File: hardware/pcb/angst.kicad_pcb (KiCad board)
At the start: 2 copper layers, 50.8 x 50.8 mm, 86 parts, among them J1 USB_B_Micro, J2 Conn_02x05_Odd_Even, J3 Conn_01x02_Male, J4 Conn_01x03, J5 Conn_01x03, J6 Conn_01x03, J7 Conn_01x02_Male, J8 Conn_01x04_Male, J9 Conn_01x02_Male, Q1 IRLML6401TRPBF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

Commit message: Add initial placement of components on layout
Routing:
- net PC0: track 24.6 -> 0.22 mm, vias 2 -> 0
- net /OUTV_1: track 18.3 -> 0.00 mm, vias 2 -> 0
- net /OUTU_1: track 12.1 -> 0.00 mm
- net /OUTW_1: track 10.6 -> 0.00 mm
- net Net-(R12-Pad1): track 7.73 -> 0.23 mm
- net PA4: track 0.00 -> 5.08 mm
- net PA5: track 0.00 -> 5.04 mm
- net PA6: track 0.00 -> 5.00 mm
- net PA7: track 0.00 -> 4.96 mm
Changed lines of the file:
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@@
     (thickness 1.6)
     (drawings 4)
-    (tracks 34)
+    (tracks 6)
     (zones 0)
     (modules 86)
@@
   (gr_line (start 114.3 88.9) (end 165.1 88.9) (layer Edge.Cuts) (width 0.2))
   (gr_line (start 114.3 38.1) (end 114.3 88.9) (layer Edge.Cuts) (width 0.2))
+  (segment (start 161.29 76.2) (end 156.21 76.2) (width 0.25) (layer F.Cu) (net 30))
+  (segment (start 161.29 73.7) (end 156.25 73.7) (width 0.25) (layer F.Cu) (net 31))
+  (segment (start 161.29 71.2) (end 156.29 71.2) (width 0.25) (layer F.Cu) (net 32))
+  (segment (start 161.29 68.7) (end 156.33 68.7) (width 0.25) (layer F.Cu) (net 33))
   (segment (start 126.25 46.535) (end 126.25 46.76) (width 0.25) (layer F.Cu) (net 45))
-  (segment (start 125.73 45.72) (end 126.25 46.535) (width 0.25) (layer F.Cu) (net 45))
-  (segment (start 123.19 45.72) (end 125.73 45.72) (width 0.25) (layer F.Cu) (net 45))
-  (segment (start 123.19 46.99) (end 123.19 45.72) (width 0.25) (layer F.Cu) (net 45))
-  (segment (start 125.5 48.01) (end 124.21 48.01) (width 0.25) (layer F.Cu) (net 45))
-  (segment (start 124.21 48.01) (end 123.19 46.99) (width 0.25) (layer F.Cu) (net 45))
-  (segment (start 125.275 47.51) (end 124.755 46.99) (width 0.25) (layer F.Cu) (net 58))
   (segment (start 125.5 47.51) (end 125.275 47.51) (width 0.25) (layer F.Cu) (net 58))
-  (via (at 124.46 46.99) (size 0.8) (drill 0.4) (layers F.Cu B.Cu) (net 58))
-  (segment (start 124.755 46.99) (end 124.46 46.99) (width 0.25) (layer F.Cu) (net 58))
-  (via (at 138.43 58.42) (size 0.8) (drill 0.4) (layers F.Cu B.Cu) (net 58))
-  (segment (start 133.546998 58.42) (end 138.43 58.42) (width 0.25) (layer B.Cu) (net 58))
-  (segment (start 124.46 46.99) (end 124.46 49.333002) (width 0.25) (layer B.Cu) (net 58))
-  (segment (start 124.46 49.333002) (end 133.546998 58.42) (width 0.25) (layer B.Cu) (net 58))
-  (segment (start 138.68 56.16) (end 138.68 55.285) (width 0.25) (layer F.Cu) (net 58))
-  (segment (start 138.68 57.604315) (end 138.68 56.16) (width 0.25) (layer F.Cu) (net 58))
-  (segment (start 138.43 57.854315) (end 138.68 57.604315) (width 0.25) (layer F.Cu) (net 58))
-  (segment (start 138.43 58.42) (end 138.43 57.854315) (width 0.25) (layer F.Cu) (net 58))
-  (segment (start 129.46 41.865) (end 130.81 43.215) (width 0.25) (layer F.Cu) (net 81))
-  (segment (start 129.46 40.64) (end 129.46 41.865) (width 0.25) (layer F.Cu) (net 81))
-  (segment (start 130.81 43.215) (end 130.81 48.26) (width 0.25) (layer F.Cu) (net 81))
-  (segment (start 130.56 48.51) (end 128.5 48.51) (width 0.25) (layer F.Cu) (net 81))
-  (segment (start 130.81 48.26) (end 130.56 48.51) (width 0.25) (layer F.Cu) (net 81))
-  (via (at 127 43.18) (size 0.8) (drill 0.4) (layers F.Cu B.Cu) (net 82))
-  (segment (start 126.96 40.64) (end 126.96 43.14) (width 0.25) (layer F.Cu) (net 82))
-  (segment (start 126.96 43.14) (end 127 43.18) (width 0.25) (layer F.Cu) (net 82))
-  (via (at 129.54 53.34) (size 0.8) (drill 0.4) (layers F.Cu B.Cu) (net 82))
-  (segment (start 127 43.18) (end 129.54 45.72) (width 0.25) (layer B.Cu) (net 82))
-  (segment (start 129.54 45.72) (end 129.54 53.34) (width 0.25) (layer B.Cu) (net 82))
-  (segment (start 127.25 51.05) (end 127.25 49.76) (width 0.25) (layer F.Cu) (net 82))
-  (segment (start 129.54 53.34) (end 127.25 51.05) (width 0.25) (layer F.Cu) (net 82))
-  (segment (start 125.5 48.51) (end 122.17 48.51) (width 0.25) (layer F.Cu) (net 83))
-  (segment (start 122.17 42.93) (end 124.46 40.64) (width 0.25) (layer F.Cu) (net 83))
-  (segment (start 122.17 48.51) (end 122.17 42.93) (width 0.25) (layer F.Cu) (net 83))
 )

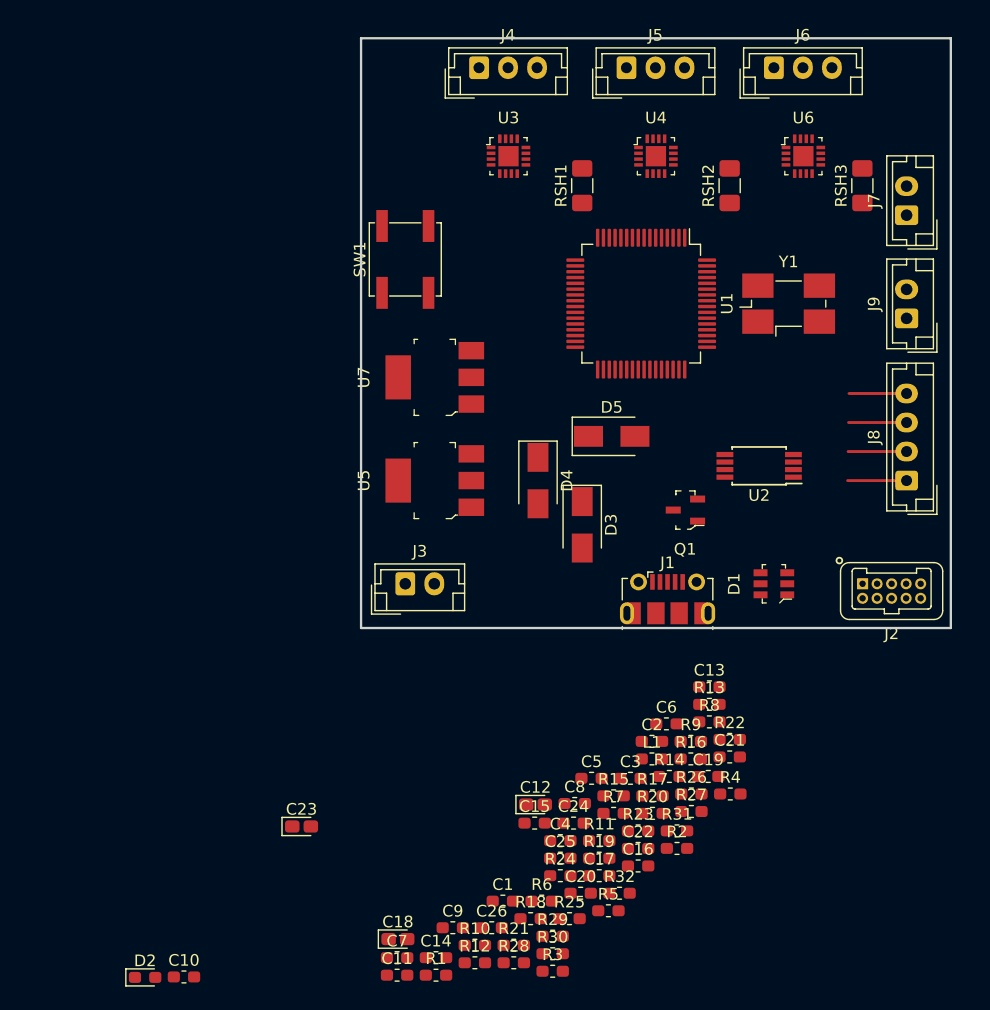
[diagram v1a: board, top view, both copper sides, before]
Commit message: Continue work on power block layout
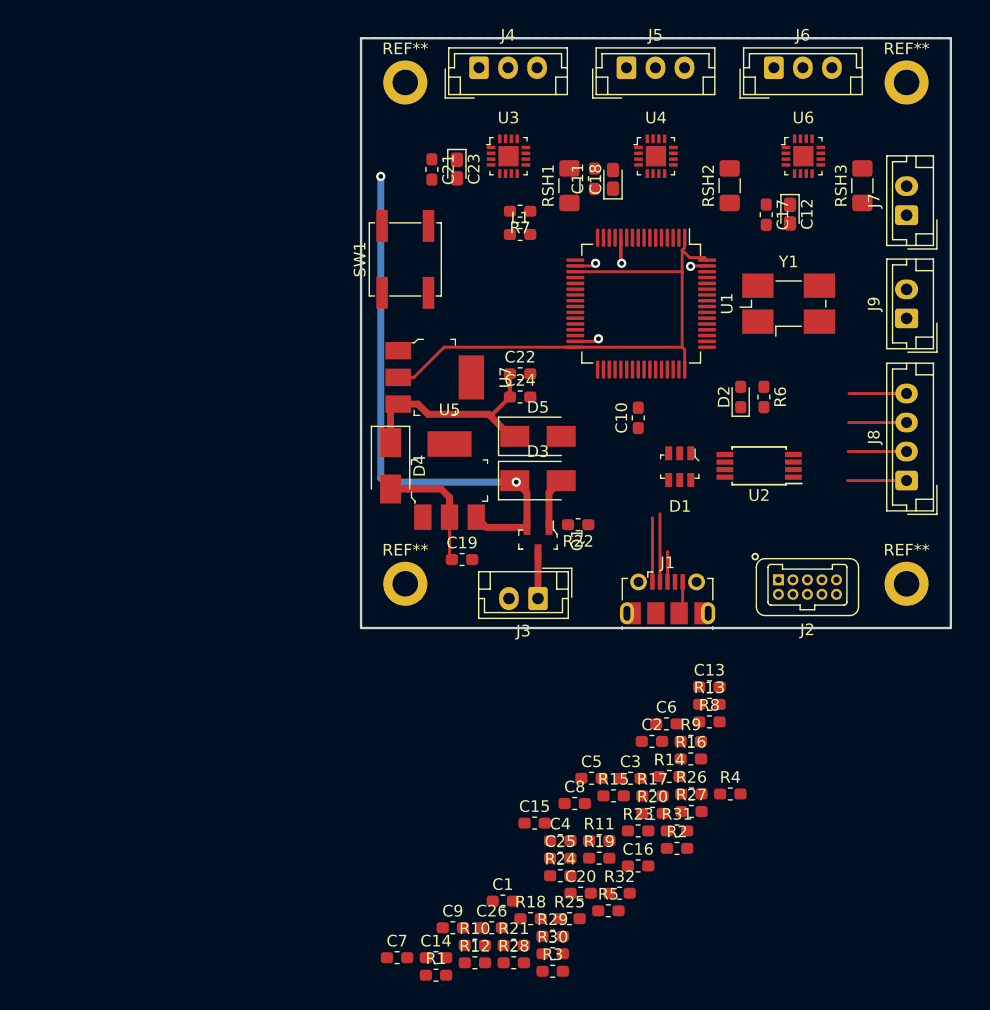
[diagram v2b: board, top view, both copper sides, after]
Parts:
- added REF**: MountingHole_2.2mm_M2_DIN965_Pad, MountingHole:MountingHole_2.2mm_M2_DIN965_Pad, F.Cu at (118.1, 85.1)
- added REF**: MountingHole_2.2mm_M2_DIN965_Pad, MountingHole:MountingHole_2.2mm_M2_DIN965_Pad, F.Cu at (161.3, 85.1)
- added REF**: MountingHole_2.2mm_M2_DIN965_Pad, MountingHole:MountingHole_2.2mm_M2_DIN965_Pad, F.Cu at (161.3, 41.9)
- added REF**: MountingHole_2.2mm_M2_DIN965_Pad, MountingHole:MountingHole_2.2mm_M2_DIN965_Pad, F.Cu at (118.1, 41.9)
- moved D2 71.6 mm to (147.0, 69.0), turned to 90 degrees
- moved C11 70.7 mm to (134.4, 50.2), turned to 90 degrees
- moved C18 68.0 mm to (136.0, 50.2), turned to 90 degrees
- moved C10 62.0 mm to (138.2, 70.8), turned to 90 degrees
- moved C17 58.7 mm to (149.2, 53.3), turned to 270 degrees
- moved C23 58.2 mm to (122.6, 49.4), turned to 270 degrees
- moved C21 56.7 mm to (120.4, 49.4), turned to 270 degrees
- moved C12 55.4 mm to (151.2, 53.2), turned to 270 degrees
- moved R7 52.5 mm to (128.0, 53.0), turned to 180 degrees
- moved R6 47.5 mm to (149.0, 69.0), turned to 270 degrees
- moved L1 46.6 mm to (128.0, 55.0)
- moved C22 42.1 mm to (128.0, 67.0)
- moved C24 37.0 mm to (128.0, 69.0)
- moved C19 28.3 mm to (123.0, 83.0)
- moved R22 22.6 mm to (133.0, 80.0), turned to 180 degrees
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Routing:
- net +3V3: track 0.00 -> 48.8 mm
- net +BATT: track 0.00 -> 47.0 mm, vias 0 -> 2
- net Net-(C22-Pad1): track 0.00 -> 19.2 mm
- net GND: track 0.00 -> 12.3 mm, vias 0 -> 4
- net +5V: track 0.00 -> 11.2 mm
- net /DM: track 0.00 -> 5.88 mm
- net +5VD: track 0.00 -> 5.53 mm
- net Net-(D3-Pad2): track 0.00 -> 4.46 mm
- net Net-(J3-Pad1): track 0.00 -> 4.03 mm
- net /DP: track 0.00 -> 2.63 mm
- added copper zone on B.Cu, net GND
- added copper zone on F.Cu, net GND

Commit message: Add work on drivers
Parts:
- moved C9 66.0 mm to (144.1, 52.5), turned to 90 degrees
- moved R30 63.0 mm to (127.0, 54.1), turned to 270 degrees
- moved R25 62.3 mm to (131.9, 51.6)
- moved R29 61.7 mm to (124.2, 54.1), turned to 270 degrees
- moved C1 60.4 mm to (135.3, 52.7)
- moved R27 58.4 mm to (134.5, 46.9), turned to 180 degrees
- moved C20 58.1 mm to (125.6, 54.1), turned to 90 degrees
- moved R9 56.3 mm to (86.6, 93.7)
- moved C5 55.9 mm to (96.0, 61.0)
- moved C26 55.8 mm to (126.9, 58.9), turned to 270 degrees
- moved R28 55.7 mm to (121.2, 62.4), turned to 270 degrees
- moved C7 55.7 mm to (125.4, 62.2), turned to 270 degrees
- moved C15 54.0 mm to (121.5, 52.3)
- moved C8 53.1 mm to (145.6, 52.5), turned to 270 degrees
- moved R13 52.8 mm to (91.7, 100.4)
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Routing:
- net +BATT: track 47.0 -> 108.5 mm, vias 2 -> 8
- net +3V3: track 48.8 -> 71.5 mm
- net PB11: track 0.00 -> 16.0 mm
- net PC14: track 0.00 -> 15.9 mm, vias 0 -> 2
- net PA3: track 0.00 -> 15.1 mm, vias 0 -> 3
- net PC3: track 0.00 -> 14.9 mm, vias 0 -> 3
- net Net-(R29-Pad1): track 0.00 -> 14.8 mm, vias 0 -> 4
- net PA2: track 0.00 -> 14.7 mm, vias 0 -> 2
- net Net-(R25-Pad1): track 0.00 -> 14.1 mm, vias 0 -> 4
- net +5VD: track 5.53 -> 19.5 mm
- net PA0: track 0.00 -> 11.6 mm
- net PA1: track 0.00 -> 10.9 mm
- net GND: track 12.3 -> 22.4 mm, vias 4 -> 14
- net Net-(R23-Pad1): track 0.00 -> 9.47 mm, vias 0 -> 3
- net /OUTU_2: track 0.00 -> 9.29 mm
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
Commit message: Continue layout
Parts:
- moved R13 81.3 mm to (158.3, 53.8), turned to 270 degrees
- moved R1 73.6 mm to (159.4, 56.1)
- moved R9 70.2 mm to (150.0, 63.6), turned to 270 degrees
- moved R12 67.9 mm to (146.8, 53.7), turned to 270 degrees
- moved R19 64.7 mm to (155.7, 49.9)
- moved R18 63.8 mm to (149.9, 53.7), turned to 270 degrees
- moved R24 61.1 mm to (154.4, 53.8), turned to 270 degrees
- moved R16 55.9 mm to (144.5, 44.3), turned to 90 degrees
- moved SW1 54.9 mm to (152.7, 83.3), turned to 180 degrees
- moved R8 54.8 mm to (146.5, 78.8), turned to 180 degrees
- moved C5 54.1 mm to (146.5, 80.3)
- moved R20 52.5 mm to (151.4, 53.7), turned to 90 degrees
- moved R10 52.1 mm to (148.5, 63.6), turned to 270 degrees
- moved J8 49.5 mm to (118.2, 51.7), turned to 270 degrees
- moved R3 48.0 mm to (137.2, 70.9), turned to 90 degrees
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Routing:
- net PB0: track 0.00 -> 87.6 mm, vias 0 -> 3
- net +3V3: track 71.5 -> 113.5 mm, vias 0 -> 7
- net Net-(R23-Pad1): track 9.47 -> 51.4 mm, vias 3 -> 7
- net nRST: track 0.00 -> 37.5 mm, vias 0 -> 1
- net PC5: track 0.00 -> 30.7 mm, vias 0 -> 4
- net PC6: track 0.00 -> 28.2 mm, vias 0 -> 2
- net PC9: track 0.00 -> 28.1 mm, vias 0 -> 3
- net PC4: track 0.00 -> 25.4 mm, vias 0 -> 2
- net PC7: track 0.00 -> 24.9 mm, vias 0 -> 2
- net PC8: track 0.00 -> 24.4 mm, vias 0 -> 2
- net PB3: track 0.00 -> 24.0 mm, vias 0 -> 1
- net PB4: track 0.00 -> 21.2 mm, vias 0 -> 1
- net PB7: track 0.00 -> 18.0 mm, vias 0 -> 2
- net PB6: track 0.00 -> 18.0 mm
- net GND: track 22.4 -> 39.5 mm, vias 14 -> 23
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
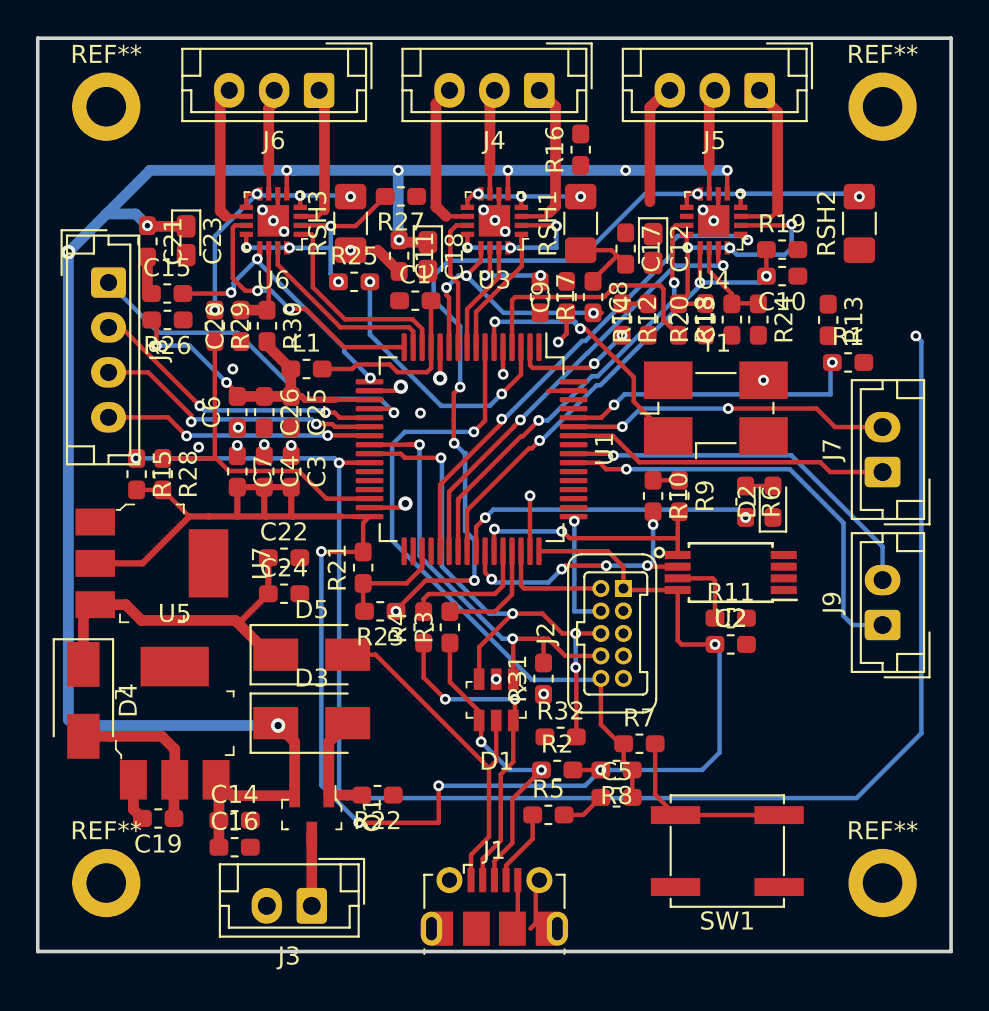
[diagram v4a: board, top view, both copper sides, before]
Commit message: Ratnest finished, start arranging graphics
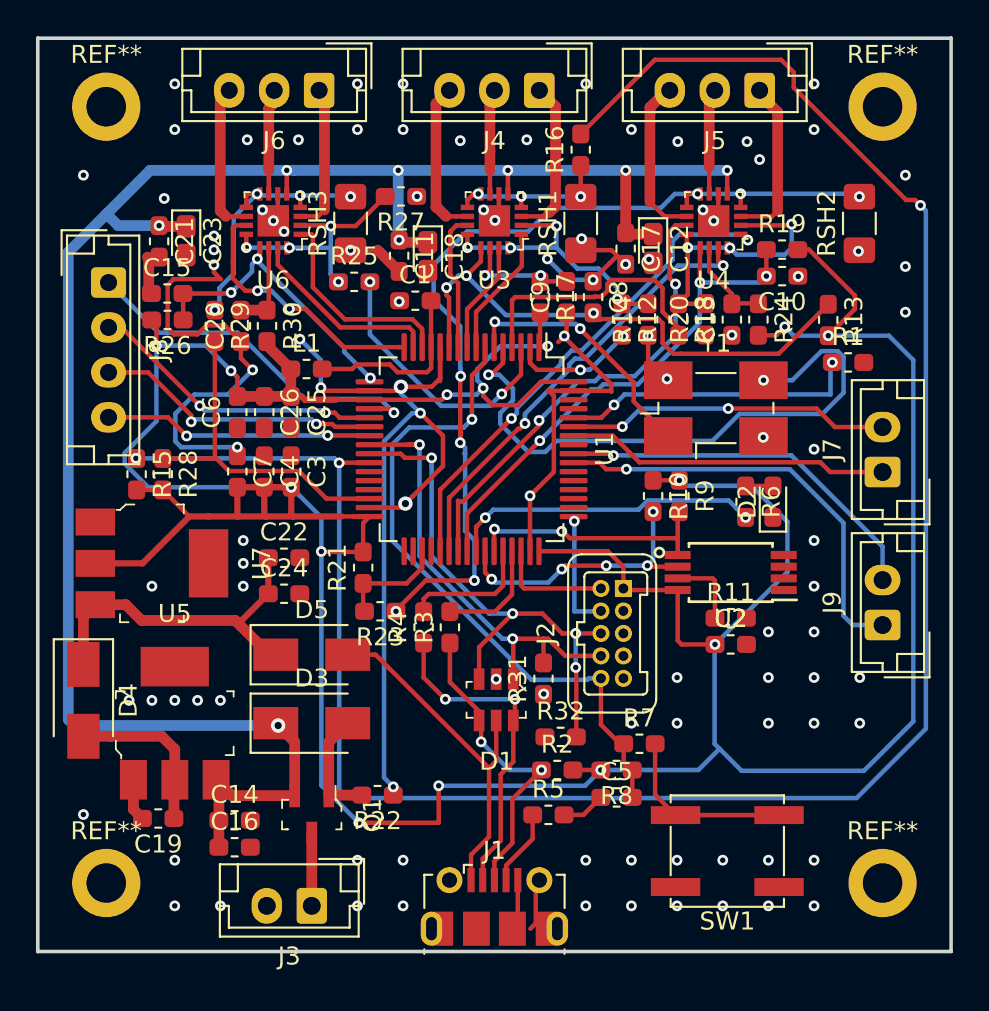
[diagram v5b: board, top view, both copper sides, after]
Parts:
- moved C21 0.65 mm to (121.0, 49.4)
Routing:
- net +3V3: track 113.5 -> 220.8 mm, vias 7 -> 14
- net GND: track 39.5 -> 120.6 mm, vias 23 -> 101
- net Net-(U1-Pad5): track 1.98 -> 34.7 mm
- net PB0: track 87.6 -> 119.4 mm
- net PC3: track 15.1 -> 31.0 mm
- net +BATT: track 103.5 -> 108.6 mm, vias 9 -> 8
- net Net-(R12-Pad1): track 10.3 -> 15.3 mm, vias 3 -> 4
- net /OUTW_2: track 6.75 -> 9.13 mm
- net Net-(R16-Pad1): track 7.67 -> 9.41 mm
- net PA3: track 15.1 -> 16.7 mm
- net PC8: track 24.4 -> 25.9 mm
- net Net-(C9-Pad2): track 4.76 -> 6.23 mm
- net PC9: track 28.1 -> 29.2 mm
- net PA9: track 15.0 -> 15.7 mm
- net Net-(R23-Pad1): track 51.4 -> 52.0 mm

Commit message: Work on layout
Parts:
- moved R28 1.57 mm to (122.8, 62.2)
- moved R15 1.54 mm to (121.3, 62.2)
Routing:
- net GND: track 120.6 -> 138.7 mm, vias 101 -> 110
- net +3V3: track 220.8 -> 218.3 mm, vias 14 -> 16
- net Net-(R23-Pad1): track 52.0 -> 53.9 mm
- net PB11: track 18.9 -> 17.4 mm
- net PB0: track 119.4 -> 117.9 mm
- net +BATT: vias 8 -> 13
